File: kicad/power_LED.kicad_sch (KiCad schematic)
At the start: 2 parts

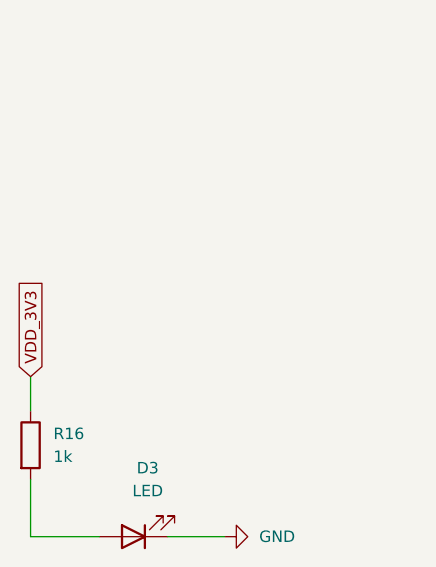
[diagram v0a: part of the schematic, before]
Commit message: feat: Update for 0.3.0 release
Add power rail controlled by PMIC load switch.
Change location for testpads to be cleaner
remove TC2030 and add JST connector for RPI debug probe
remove VDD_GPIO jumper
fix silkscreen

Signed-off-by: Bobob Bäck Engström <bobo@id8-engineering.io>
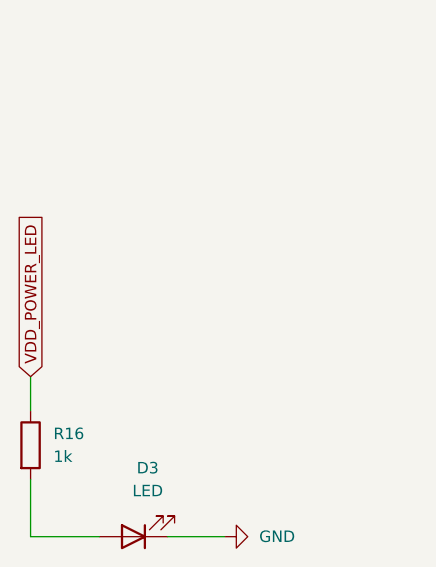
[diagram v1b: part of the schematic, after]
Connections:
- net VDD_3V3 renamed VDD_POWER_LED
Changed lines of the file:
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@@
 		)
 	)
-	(global_label "VDD_3V3"
+	(global_label "VDD_POWER_LED"
 		(shape input)
 		(at 87.63 87.63 90)
@@
 		)
 		(property "Intersheetrefs" "${INTERSHEET_REFS}"
-			(at 87.63 76.541 90)
+			(at 87.63 69.163 90)
 			(hide yes)
 			(show_name no)
